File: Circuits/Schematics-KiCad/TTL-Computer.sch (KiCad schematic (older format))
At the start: 0 parts

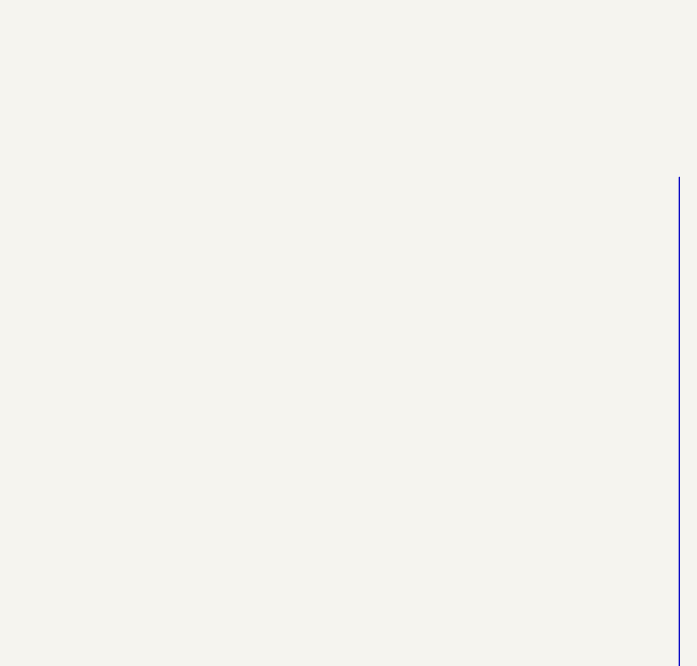
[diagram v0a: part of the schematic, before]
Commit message: Updated folder structure and working out the memory module
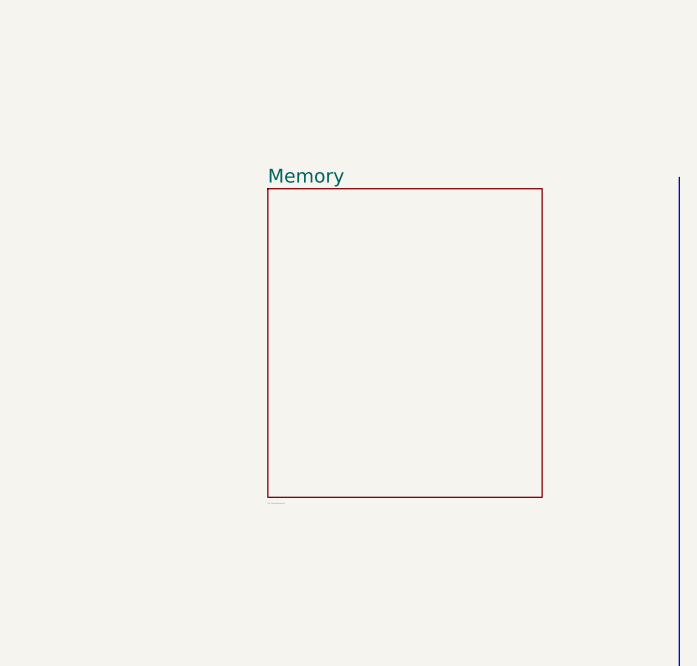
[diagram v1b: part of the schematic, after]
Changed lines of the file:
@@
 LIBS:contrib
 LIBS:valves
+LIBS:TTL-Computer-Components
 LIBS:TTL-Computer-cache
 EELAYER 25 0
@@
 $Descr A3 11693 16535 portrait
 encoding utf-8
-Sheet 1 10
+Sheet 1 11
 Title "TTL Computer"
 Date ""
@@
 Wire Wire Line
 	6600 9550 6250 9550
+$Sheet
+S 8850 2300 1200 1350
+U 5AF592F9
+F0 "Memory" 60
+F1 "./Memory/Memory.sch" 4
+$EndSheet
 $EndSCHEMATC

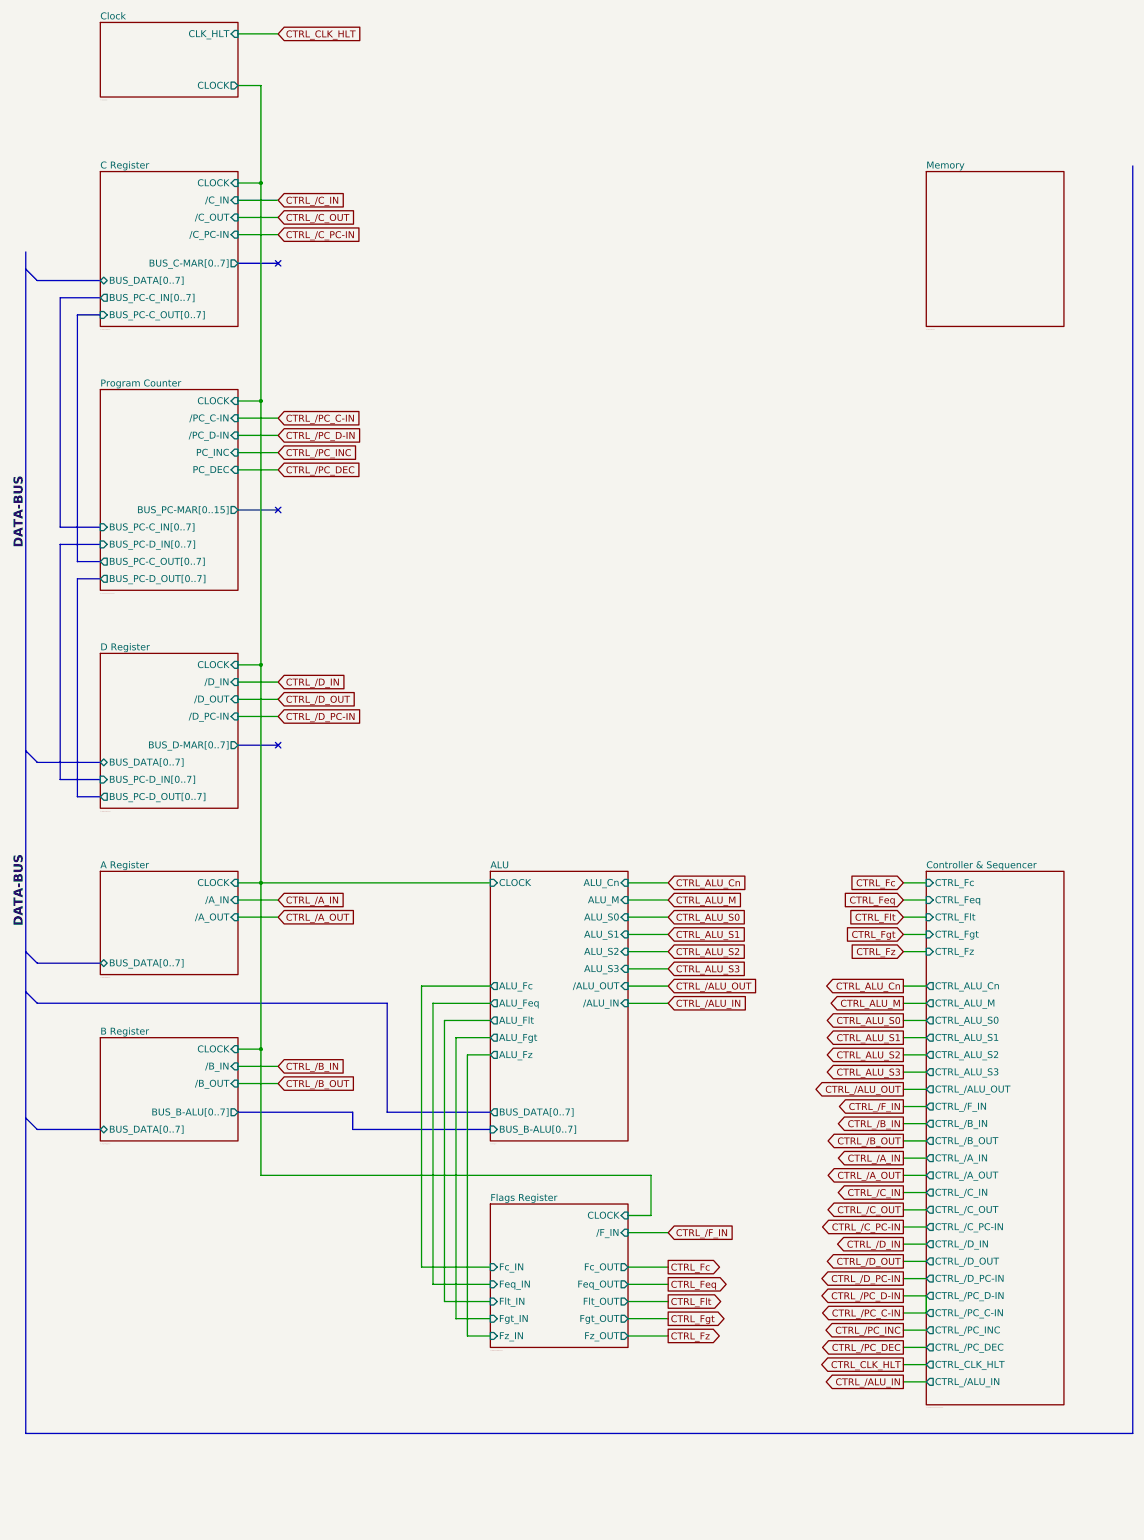
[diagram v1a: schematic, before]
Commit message: Completed memory circuit diagram (untested)
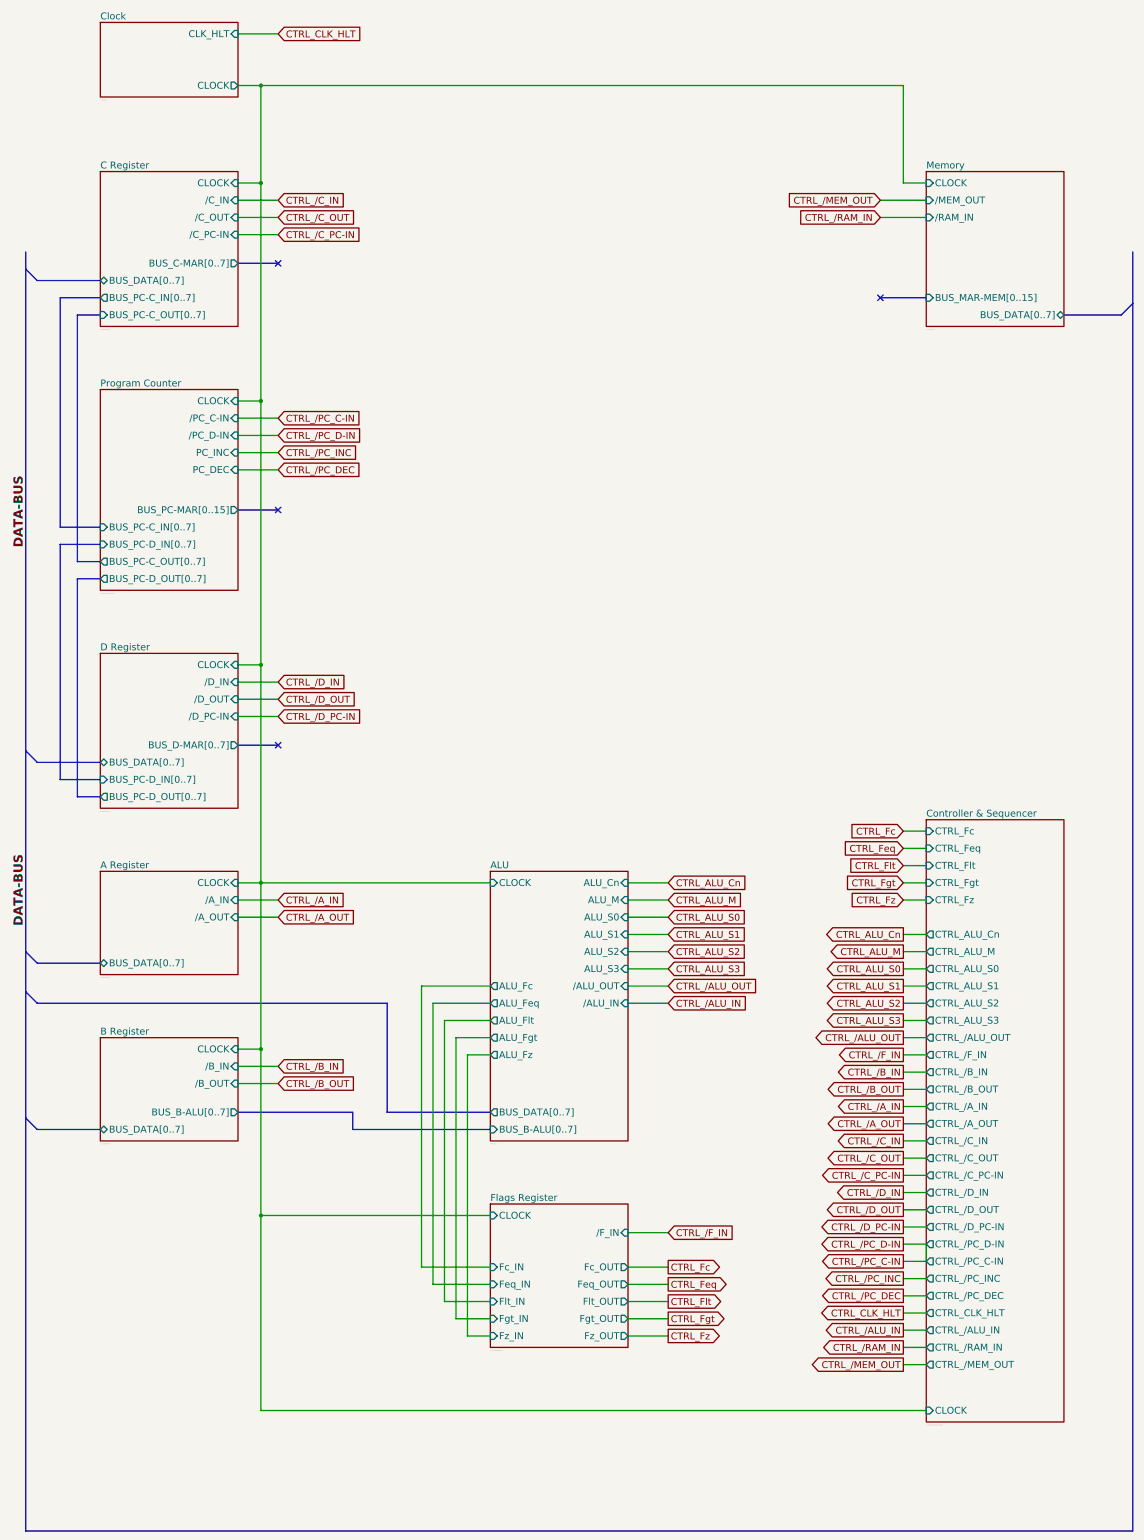
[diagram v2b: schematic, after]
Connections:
- no-connect marks 3 -> 4

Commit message: Added Stack Pointer schematic (untested)
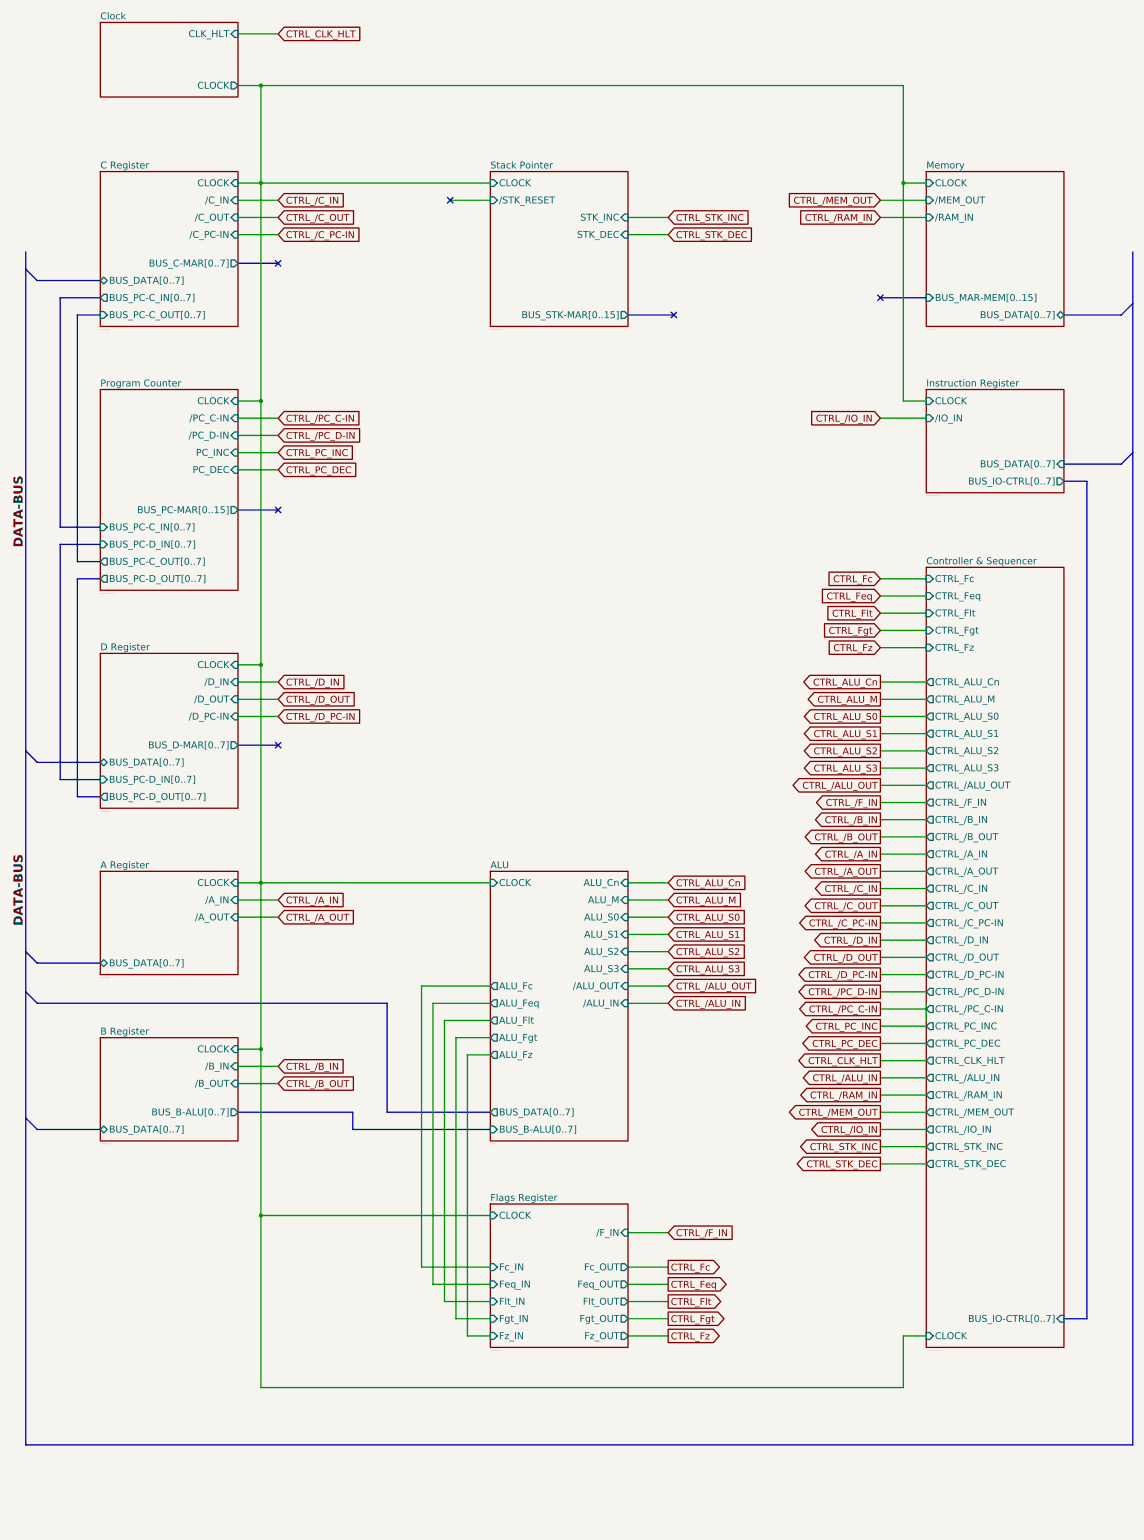
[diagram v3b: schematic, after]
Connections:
- no-connect marks 4 -> 6

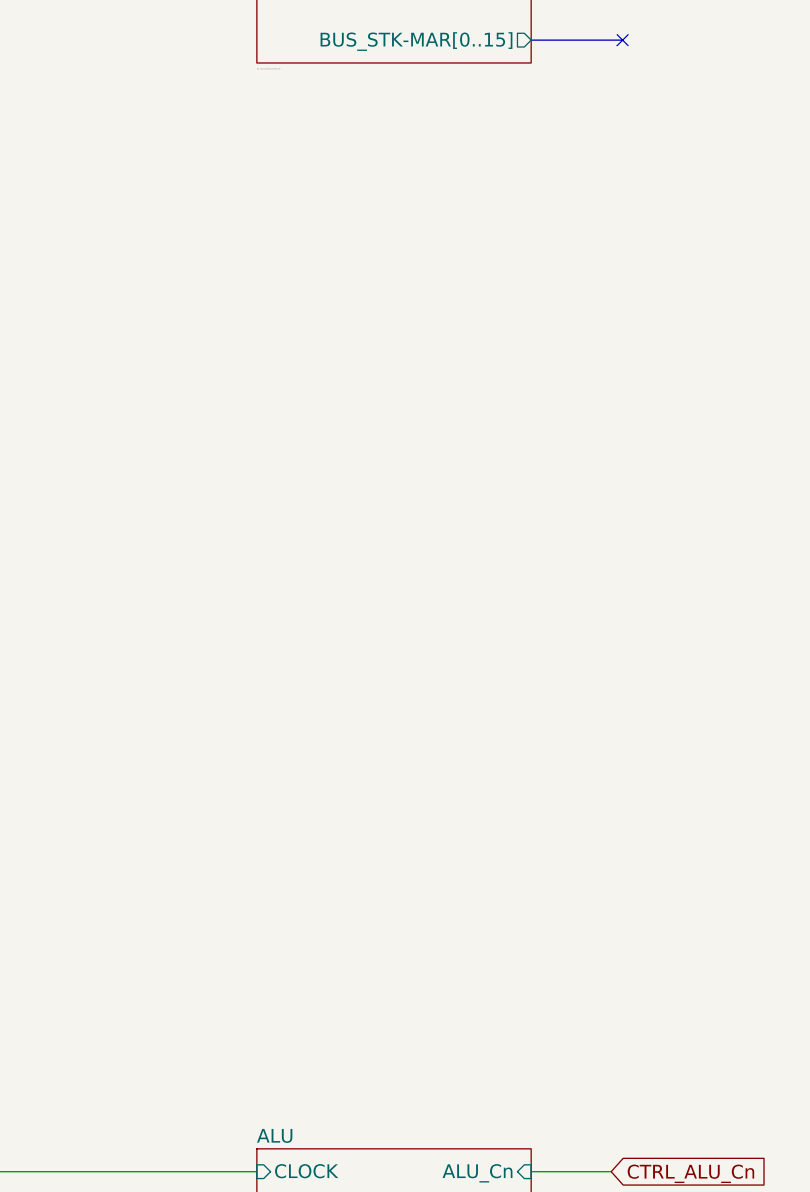
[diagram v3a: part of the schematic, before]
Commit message: Added empty MAR module schematic
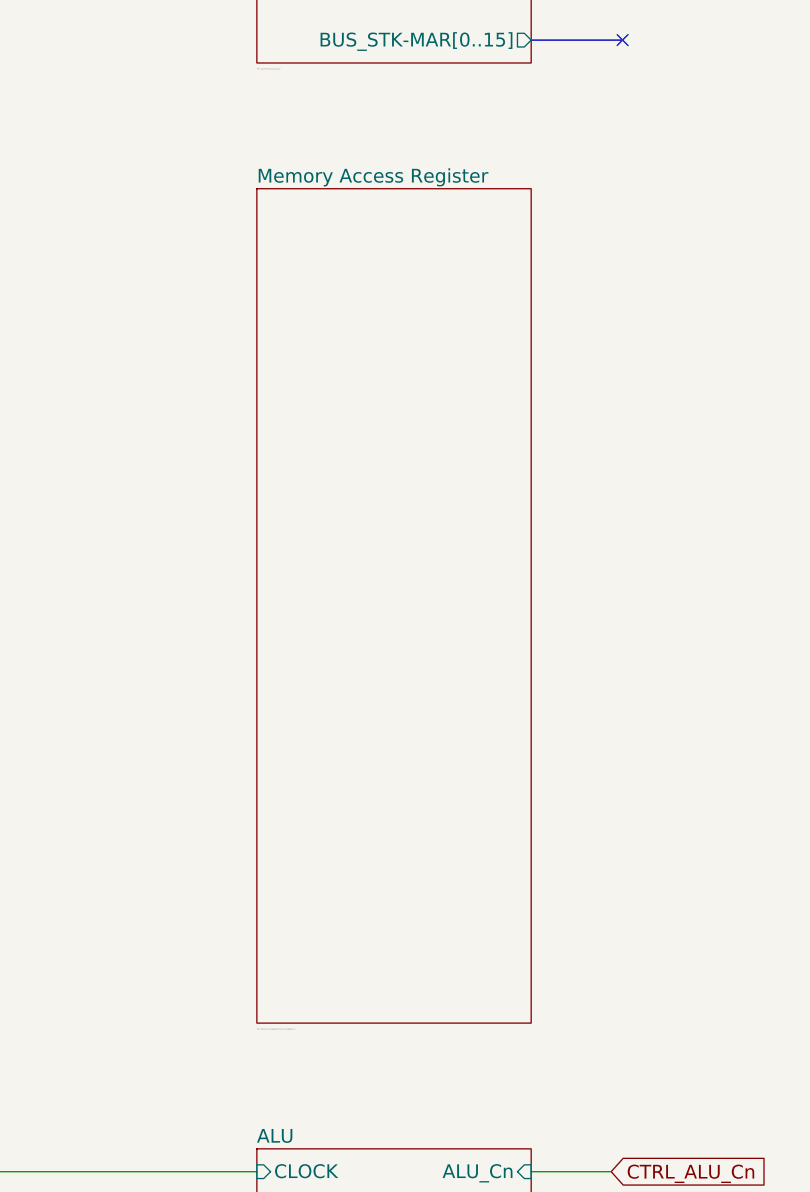
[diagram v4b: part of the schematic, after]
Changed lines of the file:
@@
 $Descr A3 11693 16535 portrait
 encoding utf-8
-Sheet 1 13
+Sheet 1 14
 Title "TTL Computer"
 Date ""
@@
 	6250 3550 6650 3550
 NoConn ~ 6650 3550
+$Sheet
+S 5050 4200 1200 3650
+U 5AF9FF2F
+F0 "Memory Access Register" 60
+F1 "./Memory-Access-Register/Memory-Access-Register.sch" 4
+$EndSheet
 $EndSCHEMATC

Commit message: Finished MAR
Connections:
- no-connect marks 6 -> 1
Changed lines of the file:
@@
 Text GLabel 3200 4900 2    60   Input ~ 0
 CTRL_PC_DEC
-NoConn ~ 3200 3100
-NoConn ~ 3200 5250
 Text GLabel 3200 6750 2    60   Input ~ 0
 CTRL_/D_IN
@@
 Text GLabel 3200 7050 2    60   Input ~ 0
 CTRL_/D_PC-IN
-NoConn ~ 3200 7300
 Text GLabel 3200 8650 2    60   Input ~ 0
 CTRL_/A_IN
@@
 Entry Bus Bus
 	10550 3550 10650 3450
-NoConn ~ 8450 3400
 $Sheet
 S 8850 4200 1200 900
@@
 F36 "CTRL_STK_INC" O L 8850 10800 60
 F37 "CTRL_STK_DEC" O L 8850 10950 60
+F38 "CTRL_/MAR_C-IN" O L 8850 11100 60
+F39 "CTRL_/MAR_D-IN" O L 8850 11250 60
+F40 "CTRL_/MAR_PC-IN" O L 8850 11400 60
+F41 "CTRL_/MAR_STK-IN" O L 8850 11550 60
 $EndSheet
 Wire Bus Line
@@
 	2850 2400 5050 2400
 Wire Wire Line
-	3050 4300 2850 4300
+	2850 4300 5050 4300
 Connection ~ 3050 2400
 Wire Bus Line
@@
 	3200 4900 2850 4900
 Wire Bus Line
-	2850 3100 3200 3100
+	2850 3100 4750 3100
 Wire Bus Line
 	2850 5250 3200 5250
@@
 	2850 7050 3200 7050
 Wire Bus Line
-	2850 7300 3200 7300
+	2850 7300 3300 7300
 Wire Wire Line
 	2850 8650 3200 8650
@@
 	10550 3550 10050 3550
 Wire Bus Line
-	8850 3400 8450 3400
+	7750 3400 8850 3400
 Wire Wire Line
 	3050 11400 5050 11400
@@
 	6600 2850 6250 2850
 Wire Bus Line
-	6250 3550 6650 3550
-NoConn ~ 6650 3550
+	6250 3550 7600 3550
 $Sheet
 S 5050 4200 1200 3650
@@
 F0 "Memory Access Register" 60
 F1 "./Memory-Access-Register/Memory-Access-Register.sch" 4
+F2 "CLOCK" I L 5050 4300 60
+F3 "BUS_C-MAR[0..7]" I L 5050 5250 60
+F4 "/MAR_D-IN" I R 6250 4600 60
+F5 "BUS_MAR-MEM[0..15]" O R 6250 5850 60
+F6 "BUS_D-MAR[0..7]" I L 5050 5550 60
+F7 "BUS_PC-MAR[0..15]" I L 5050 5400 60
+F8 "BUS_STK-MAR[0..15]" I R 6250 5700 60
+F9 "/MAR_C-IN" I R 6250 4450 60
+F10 "/MAR_PC-IN" I R 6250 4750 60
+F11 "/MAR_STK-IN" I R 6250 4900 60
 $EndSheet
+Text Label 10650 10750 1    79   ~ 16
+DATA-BUS
+Text Label 10650 5400 3    79   ~ 16
+DATA-BUS
+Text Label 6250 13400 2    79   ~ 16
+DATA-BUS
+Wire Bus Line
+	7600 3550 7600 5700
+Wire Bus Line
+	7600 5700 6250 5700
+Wire Bus Line
+	7750 3400 7750 5850
+Wire Bus Line
+	7750 5850 6250 5850
+Wire Bus Line
+	4750 3100 4750 5250
+Wire Bus Line
+	4750 5250 5050 5250
+Wire Bus Line
+	3250 7300 4750 7300
+Wire Bus Line
+	4750 7300 4750 5550
+Wire Bus Line
+	4750 5550 5050 5550
+Wire Bus Line
+	5050 5400 3200 5400
+Wire Bus Line
+	3200 5400 3200 5250
+Text GLabel 6600 4450 2    60   Input ~ 0
+CTRL_/MAR_C-IN
+Text GLabel 6600 4600 2    60   Input ~ 0
+CTRL_/MAR_D-IN
+Text GLabel 6600 4750 2    60   Input ~ 0
+CTRL_/MAR_PC-IN
+Text GLabel 6600 4900 2    60   Input ~ 0
+CTRL_/MAR_STK-IN
+Wire Wire Line
+	6250 4450 6600 4450
+Wire Wire Line
+	6600 4600 6250 4600
+Wire Wire Line
+	6250 4750 6600 4750
+Wire Wire Line
+	6600 4900 6250 4900
+Text GLabel 8450 11100 0    60   Output ~ 0
+CTRL_/MAR_C-IN
+Text GLabel 8450 11250 0    60   Output ~ 0
+CTRL_/MAR_D-IN
+Text GLabel 8450 11400 0    60   Output ~ 0
+CTRL_/MAR_PC-IN
+Text GLabel 8450 11550 0    60   Output ~ 0
+CTRL_/MAR_STK-IN
+Wire Wire Line
+	8450 11100 8850 11100
+Wire Wire Line
+	8850 11250 8450 11250
+Wire Wire Line
+	8450 11400 8850 11400
+Wire Wire Line
+	8850 11550 8450 11550
 $EndSCHEMATC
